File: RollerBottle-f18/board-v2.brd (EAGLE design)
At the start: 160 x 100 mm, 23 parts, among them IC1 7805T, J1 POWER_JACKPTH_BREAD, U1 328P

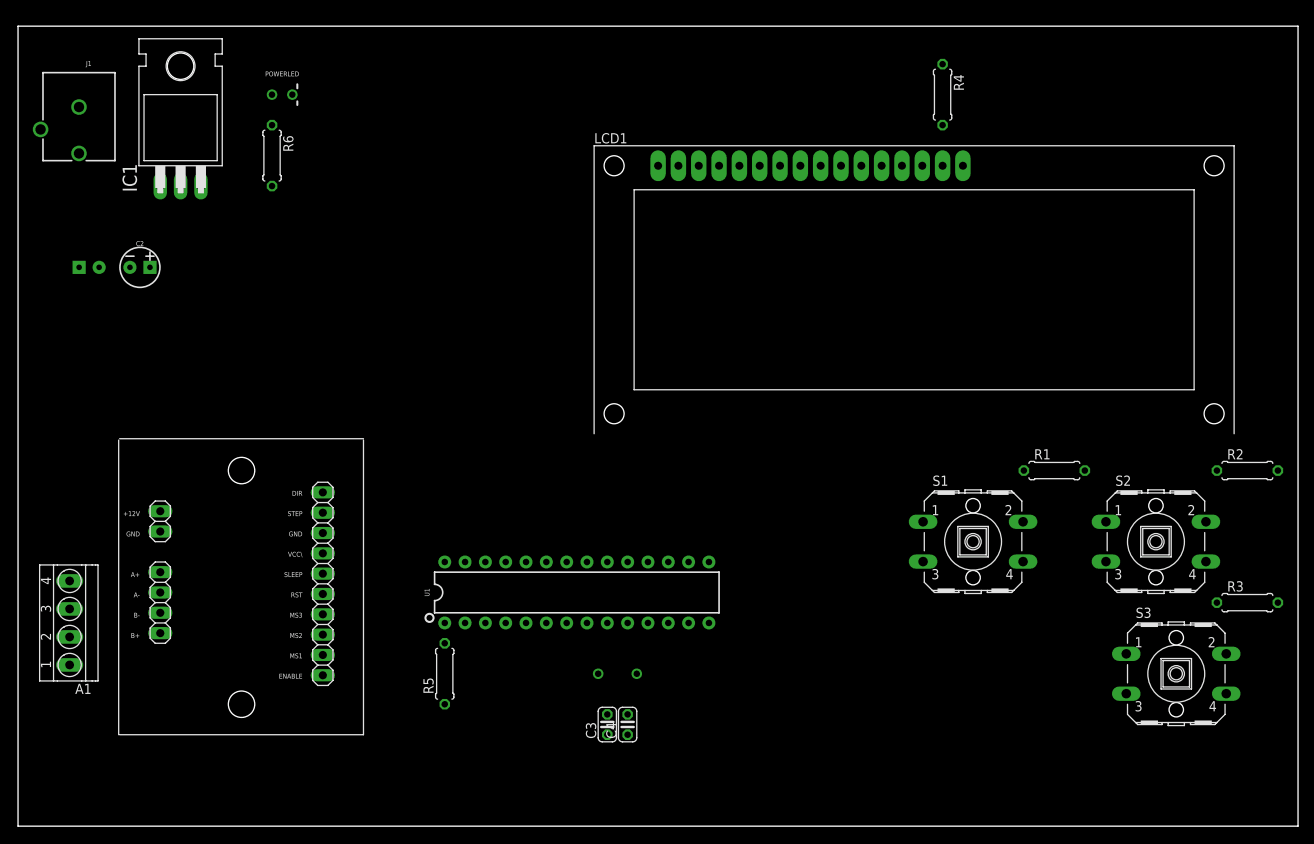
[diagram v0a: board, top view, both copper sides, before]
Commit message: Traces added
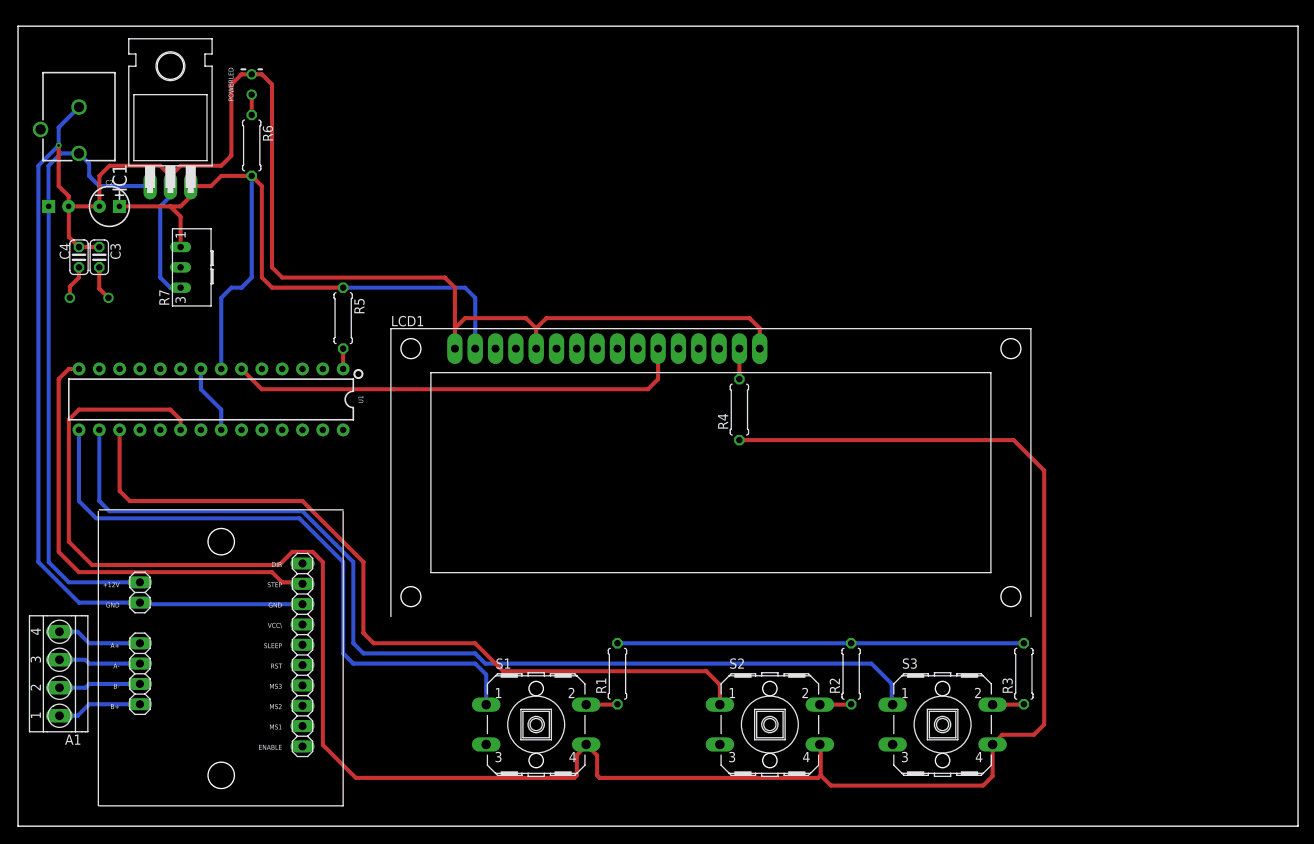
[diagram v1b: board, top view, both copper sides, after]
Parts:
- added R7: (no value), pot:S63S
- moved C4 90.1 mm to (7.62, 71.1), turned to 270 degrees
- moved C3 86.3 mm to (10.2, 71.1), turned to 270 degrees
- moved Q1 81.1 mm to (8.89, 66.0), turned to 180 degrees
- moved R1 60.2 mm to (74.9, 19.1), turned to 90 degrees
- moved S1 59.2 mm to (64.8, 12.7)
- moved R2 55.7 mm to (104.1, 19.1), turned to 90 degrees
- moved S2 53.4 mm to (94.0, 12.7)
- moved U1 51.7 mm to (24.1, 53.3), turned to 180 degrees
- moved R4 46.9 mm to (90.2, 52.1), turned to 90 degrees
- moved R5 46.2 mm to (40.6, 63.5), turned to 270 degrees
- moved LCD1 34.2 mm to (52.1, 59.7)
- moved S3 29.9 mm to (115.6, 12.7)
- moved R3 29.3 mm to (125.7, 19.1), turned to 90 degrees
- moved JP4 9.25 mm to (35.6, 21.4)
- moved JP5 9.25 mm to (15.2, 29.2)
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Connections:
- removed net M_+12V: JP5.1
- removed net M_GND: JP4.3, JP5.2
- removed net N$5: LCD1.4
- removed net N$6: LCD1.5
- removed net N$7: LCD1.6
- removed net STEP: U1.14
- new net PB4: LCD1.6, U1.18
- new net PB5: LCD1.4, U1.19
- net +12V: now also JP5.1
- net +5V: now also R7.A
- net GND: now also JP4.3, JP5.2, LCD1.5, R7.E
- net M_STEP: now also U1.14
- net N$2: now also R7.S
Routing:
- net +5V: track 0.00 -> 366.6 mm
- net GND: track 0.00 -> 327.2 mm, vias 0 -> 2
- net MINUS: track 0.00 -> 125.9 mm
- net PLUS: track 0.00 -> 100.4 mm
- net MODE: track 0.00 -> 79.2 mm
- net +12V: track 0.00 -> 77.9 mm
- net DB4: track 0.00 -> 57.5 mm
- net M_STEP: track 0.00 -> 56.8 mm
- net M_A+: track 0.00 -> 10.7 mm
- net M_B+: track 0.00 -> 10.7 mm
- net M_B-: track 0.00 -> 10.3 mm
- net M_A-: track 0.00 -> 10.3 mm
- net N$13: track 0.00 -> 4.28 mm
- net N$1: track 0.00 -> 4.28 mm
- net N$15: track 0.00 -> 3.93 mm
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
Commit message: Backing up board v2
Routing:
- net DB7: track 0.00 -> 97.5 mm, vias 0 -> 1
- net DB6: track 0.00 -> 91.8 mm, vias 0 -> 1
- net DB5: track 0.00 -> 85.7 mm, vias 0 -> 1
- net GND: track 327.2 -> 412.4 mm, vias 2 -> 0
- net PB4: track 0.00 -> 75.2 mm
- net PB5: track 0.00 -> 65.1 mm
- net +5V: track 366.6 -> 420.7 mm
- net N$2: track 0.00 -> 52.7 mm, vias 0 -> 1
- net N$1: track 4.28 -> 22.3 mm
- net N$13: track 4.28 -> 19.9 mm
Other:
- board size 160 x 100 mm -> 133.3 x 100 mm

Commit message: Board finished
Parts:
- moved R3 14.2 mm to (111.8, 21.6)
- moved S3 11.4 mm to (104.1, 12.7)
- moved R2 10.5 mm to (94.0, 21.6)
- moved R1 7.62 mm to (67.3, 19.1)
- moved S2 7.62 mm to (86.4, 12.7)
- moved S1 7.62 mm to (57.1, 12.7)
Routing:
- net GND: track 412.4 -> 374.8 mm
- net +5V: track 420.7 -> 395.3 mm
- net MINUS: track 126.0 -> 114.6 mm
- net PLUS: track 100.4 -> 92.8 mm
- net MODE: track 79.2 -> 71.6 mm
- net DB7: track 97.5 -> 98.5 mm
- net +12V: track 77.9 -> 79.0 mm
- net M_STEP: track 56.8 -> 57.8 mm
- net N$15: track 3.93 -> 3.16 mm
- net N$16: track 3.93 -> 3.16 mm
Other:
- board size 133.3 x 100 mm -> 133.3 x 101.3 mm
